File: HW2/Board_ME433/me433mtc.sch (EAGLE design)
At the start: 19 parts, among them IC2 MCP1702, J1 USBMINIB-MB-H, SW1 SLIDE

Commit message: finished schematic
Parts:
- added C1: 0.1uF, mtcboard:C-US025-025X050
- added IC1: PIC32MX250F128B, mtcboard:PIC32
- added Y1: 8MHz, mtcboard:RESONATOR
- R1, R2: value (none) -> 330
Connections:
- new net A0: IC1.2.A0, J4.8
- new net A1: IC1.3.A1, J4.7
- new net B2: IC1.6.B2, J4.6
- new net B3: IC1.7.B3, J4.5
- new net B4/LED: IC1.11.B4
- new net N$1: IC1.9.A2, Y1.1.OSC1
- new net N$13: IC1.10.A3, Y1.3.OSC2
- new net N$16: C3.1, IC1.13.VDD
- new net N$7: C7.+, IC1.20.VCAP
- net +3V3: now also C1.1, IC1.23.VUSB3V3, IC1.28.AVDD, J4.2
- net +5V: now also IC1.15.VBUS
- net A4/LED: now also IC1.12.A4, J4.3
- net B13: now also IC1.24.B13
- net B14: now also IC1.25.B14
- net B15: now also IC1.26.B15
- net B4/USER: now also J4.4
- net B7: now also IC1.16.B7
- net B8: now also IC1.17.B8
- net B9: now also IC1.18.B9
- net D+: now also IC1.21.D+/B10
- net D-: now also IC1.22.D-/B11
- net GND: now also C1.2, C3.2, C7.-, IC1.19.VSS, IC1.27.AVSS, IC1.8.VSS, J4.1, Y1.2.GND
- net MCLR: now also IC1.1.MCLR
- net PGC: now also IC1.5.PGEC1/B0
- net PGD: now also IC1.4.PGED1/B0
- net USBID: now also IC1.14.USBID/B5
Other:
- moved on the sheet: C3, C7

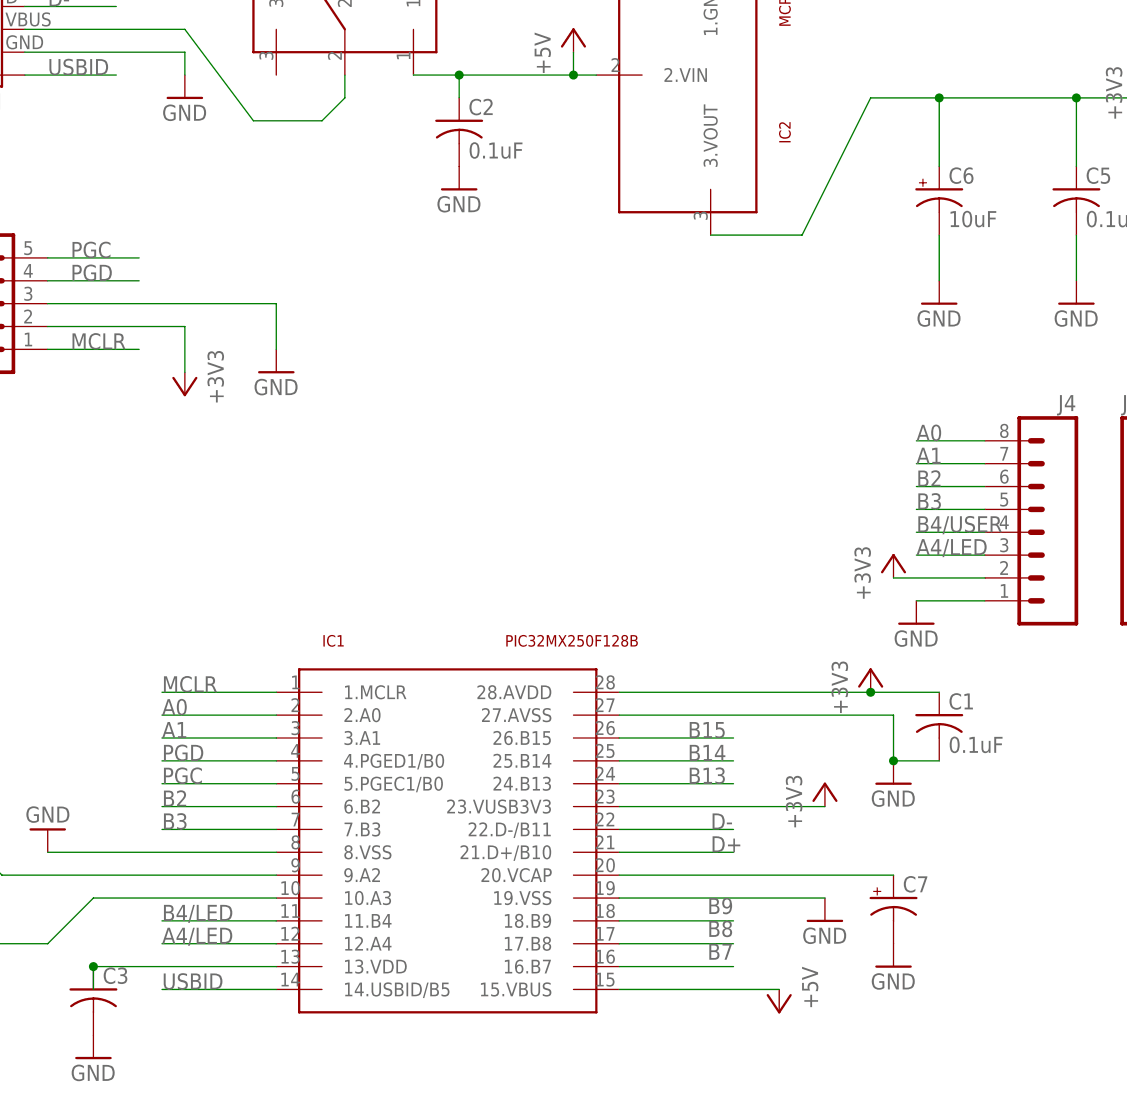
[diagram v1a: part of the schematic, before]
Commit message: board is placed
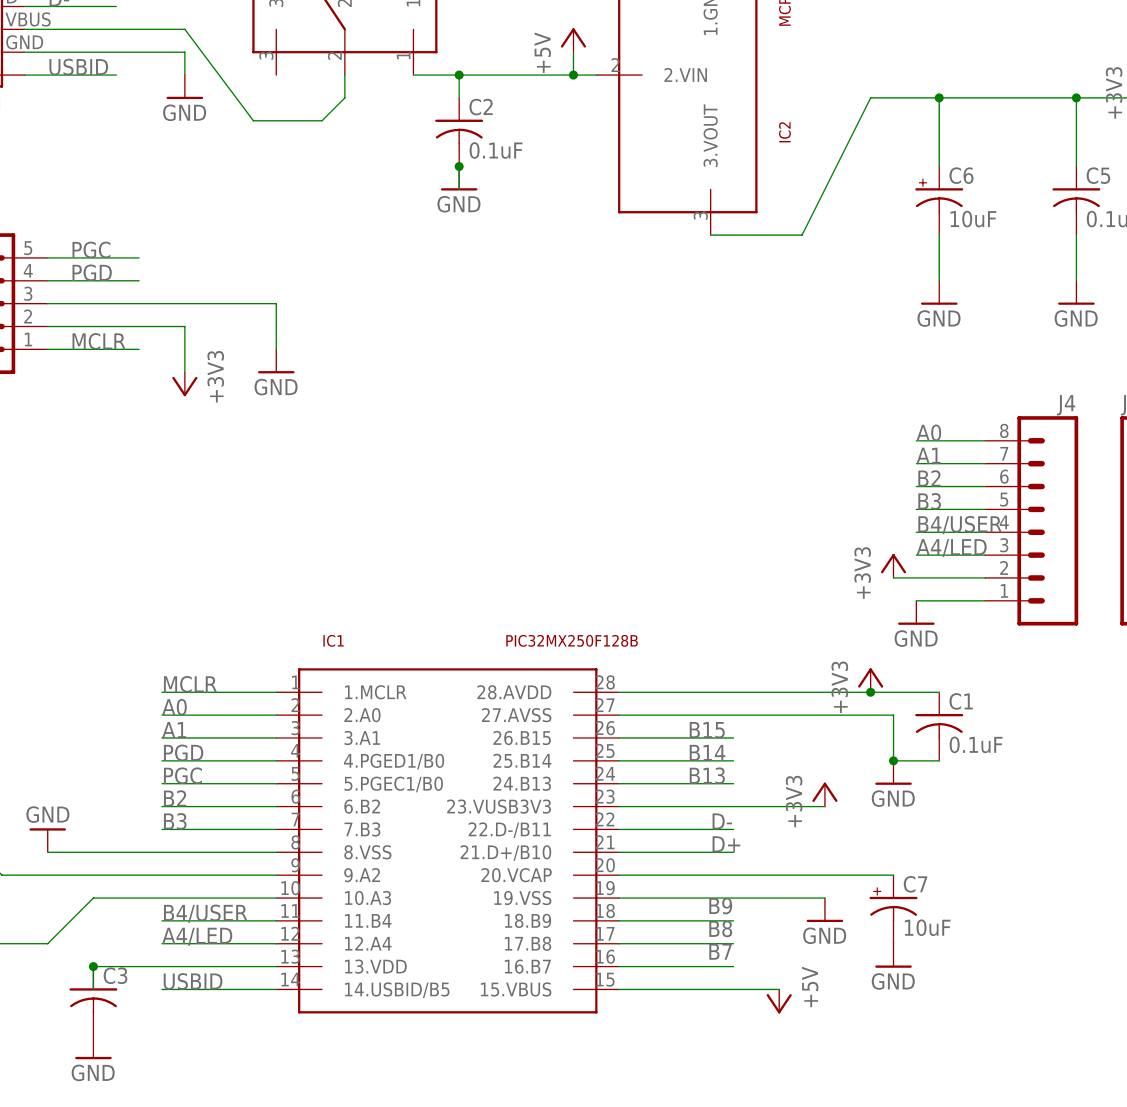
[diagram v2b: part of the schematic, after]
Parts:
- C7: value (none) -> 10uF
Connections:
- removed net B4/LED: IC1.11.B4
- net B4/USER: now also IC1.11.B4
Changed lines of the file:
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@@
 <part name="IC2" library="mtcboard" deviceset="MCP1702" device=""/>
 <part name="GND1" library="mtcboard" deviceset="GND" device=""/>
-<part name="GND2" library="mtcboard" deviceset="GND" device=""/>
 <part name="GND3" library="mtcboard" deviceset="GND" device=""/>
 <part name="GND4" library="mtcboard" deviceset="GND" device=""/>
@@
 <part name="C5" library="mtcboard" deviceset="C-US" device="025-025X050" value="0.1uF"/>
 <part name="C6" library="mtcboard" deviceset="CPOL-US" device="B45181B" value="10uF"/>
-<part name="C7" library="mtcboard" deviceset="CPOL-US" device="B45181B"/>
+<part name="C7" library="mtcboard" deviceset="CPOL-US" device="B45181B" value="10uF"/>
 <part name="P+1" library="mtcboard" deviceset="+5V" device=""/>
 <part name="+3V1" library="mtcboard" deviceset="+3V3" device=""/>
@@
 <part name="+3V6" library="mtcboard" deviceset="+3V3" device=""/>
 <part name="+3V7" library="mtcboard" deviceset="+3V3" device=""/>
+<part name="GND2" library="mtcboard" deviceset="GND" device=""/>
 </parts>
 <sheets>
@@
 <instance part="IC2" gate="G$1" x="129.54" y="96.52" rot="R270"/>
 <instance part="GND1" gate="1" x="73.66" y="93.98"/>
-<instance part="GND2" gate="1" x="104.14" y="83.82"/>
 <instance part="GND3" gate="1" x="132.08" y="116.84" rot="R180"/>
 <instance part="GND4" gate="1" x="157.48" y="71.12"/>
@@
 <instance part="+3V6" gate="G$1" x="144.78" y="17.78"/>
 <instance part="+3V7" gate="G$1" x="149.86" y="30.48"/>
+<instance part="GND2" gate="1" x="104.14" y="83.82"/>
 </instances>
 <busses>
@@
 <wire x1="55.88" y1="99.06" x2="73.66" y2="99.06" width="0.1524" layer="91"/>
 <wire x1="73.66" y1="99.06" x2="73.66" y2="96.52" width="0.1524" layer="91"/>
-</segment>
-<segment>
-<pinref part="C2" gate="G$1" pin="2"/>
-<pinref part="GND2" gate="1" pin="GND"/>
 </segment>
 <segment>
@@
 <pinref part="C7" gate="G$1" pin="-"/>
 <pinref part="GND17" gate="1" pin="GND"/>
+</segment>
+<segment>
+<pinref part="C2" gate="G$1" pin="2"/>
+<wire x1="104.14" y1="83.82" x2="104.14" y2="86.36" width="0.1524" layer="91"/>
+<pinref part="GND2" gate="1" pin="GND"/>
+<junction x="104.14" y="86.36"/>
 </segment>
 </net>
@@
 <label x="154.94" y="45.72" size="1.778" layer="95"/>
 </segment>
+<segment>
+<pinref part="IC1" gate="G$1" pin="11.B4"/>
+<wire x1="83.82" y1="2.54" x2="71.12" y2="2.54" width="0.1524" layer="91"/>
+<label x="71.12" y="2.54" size="1.778" layer="95"/>
+</segment>
 </net>
 <net name="B15" class="0">
@@
 </segment>
 </net>
-<net name="B4/LED" class="0">
-<segment>
-<pinref part="IC1" gate="G$1" pin="11.B4"/>
-<wire x1="83.82" y1="2.54" x2="71.12" y2="2.54" width="0.1524" layer="91"/>
-<label x="71.12" y="2.54" size="1.778" layer="95"/>
-</segment>
-</net>

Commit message: finished board
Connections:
- removed net N$16: C3.1, IC1.13.VDD
- net +3V3: now also C3.1, IC1.13.VDD
- net A0: now also J4.A0; no longer J4.8
- net B15: now also J3.A0; no longer J3.8
- net B4/USER: now also R3.1
- net MCLR: now also R4.1
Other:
- moved on the sheet: C1
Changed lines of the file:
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@@
 <instance part="GND14" gate="1" x="58.42" y="12.7" rot="R180"/>
 <instance part="GND15" gate="1" x="43.18" y="5.08"/>
-<instance part="C1" gate="G$1" x="157.48" y="25.4"/>
+<instance part="C1" gate="G$1" x="160.02" y="25.4"/>
 <instance part="GND16" gate="1" x="152.4" y="17.78"/>
 <instance part="GND17" gate="1" x="152.4" y="-2.54"/>
@@
 <pinref part="C1" gate="G$1" pin="2"/>
 <pinref part="GND16" gate="1" pin="GND"/>
-<wire x1="152.4" y1="20.32" x2="157.48" y2="20.32" width="0.1524" layer="91"/>
+<wire x1="152.4" y1="20.32" x2="160.02" y2="20.32" width="0.1524" layer="91"/>
 <junction x="152.4" y="20.32"/>
 </segment>
@@
 <pinref part="C1" gate="G$1" pin="1"/>
 <pinref part="+3V7" gate="G$1" pin="+3V3"/>
-<wire x1="149.86" y1="27.94" x2="157.48" y2="27.94" width="0.1524" layer="91"/>
+<wire x1="149.86" y1="27.94" x2="160.02" y2="27.94" width="0.1524" layer="91"/>
 <junction x="149.86" y="27.94"/>
+</segment>
+<segment>
+<pinref part="IC1" gate="G$1" pin="13.VDD"/>
+<wire x1="83.82" y1="-2.54" x2="63.5" y2="-2.54" width="0.1524" layer="91"/>
+<wire x1="63.5" y1="-2.54" x2="63.5" y2="-5.08" width="0.1524" layer="91"/>
+<pinref part="C3" gate="G$1" pin="1"/>
+<junction x="63.5" y="-2.54"/>
 </segment>
 </net>
@@
 <segment>
 <pinref part="PB1" gate="G$1" pin="1.IN"/>
-<wire x1="246.38" y1="50.8" x2="226.06" y2="50.8" width="0.1524" layer="91"/>
+<wire x1="246.38" y1="50.8" x2="238.76" y2="50.8" width="0.1524" layer="91"/>
 <label x="223.52" y="50.8" size="1.778" layer="95"/>
+<pinref part="R4" gate="G$1" pin="1"/>
+<wire x1="238.76" y1="50.8" x2="226.06" y2="50.8" width="0.1524" layer="91"/>
+<junction x="238.76" y="50.8"/>
 </segment>
 <segment>
@@
 <segment>
 <pinref part="PB2" gate="G$1" pin="1.IN"/>
-<wire x1="248.92" y1="88.9" x2="226.06" y2="88.9" width="0.1524" layer="91"/>
+<wire x1="248.92" y1="88.9" x2="236.22" y2="88.9" width="0.1524" layer="91"/>
 <label x="220.98" y="88.9" size="1.778" layer="95"/>
+<pinref part="R3" gate="G$1" pin="1"/>
+<wire x1="236.22" y1="88.9" x2="226.06" y2="88.9" width="0.1524" layer="91"/>
+<junction x="236.22" y="88.9"/>
 </segment>
 <segment>
@@
 <net name="B15" class="0">
 <segment>
-<pinref part="J3" gate="G$1" pin="8"/>
+<pinref part="J3" gate="G$1" pin="A0"/>
 <wire x1="187.96" y1="55.88" x2="198.12" y2="55.88" width="0.1524" layer="91"/>
 <label x="190.5" y="55.88" size="1.778" layer="95"/>
@@
 <net name="A0" class="0">
 <segment>
-<pinref part="J4" gate="G$1" pin="8"/>
+<pinref part="J4" gate="G$1" pin="A0"/>
 <wire x1="162.56" y1="55.88" x2="154.94" y2="55.88" width="0.1524" layer="91"/>
 <label x="154.94" y="55.88" size="1.778" layer="95"/>
@@
 </segment>
 </net>
-<net name="N$16" class="0">
-<segment>
-<pinref part="IC1" gate="G$1" pin="13.VDD"/>
-<wire x1="83.82" y1="-2.54" x2="63.5" y2="-2.54" width="0.1524" layer="91"/>
-<wire x1="63.5" y1="-2.54" x2="63.5" y2="-5.08" width="0.1524" layer="91"/>
-<pinref part="C3" gate="G$1" pin="1"/>
-<junction x="63.5" y="-2.54"/>
-</segment>
-</net>
